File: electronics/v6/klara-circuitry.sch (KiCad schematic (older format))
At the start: 15 parts, among them J1 Pin header, U1 MCP1700-3302E, U3 ATtiny85

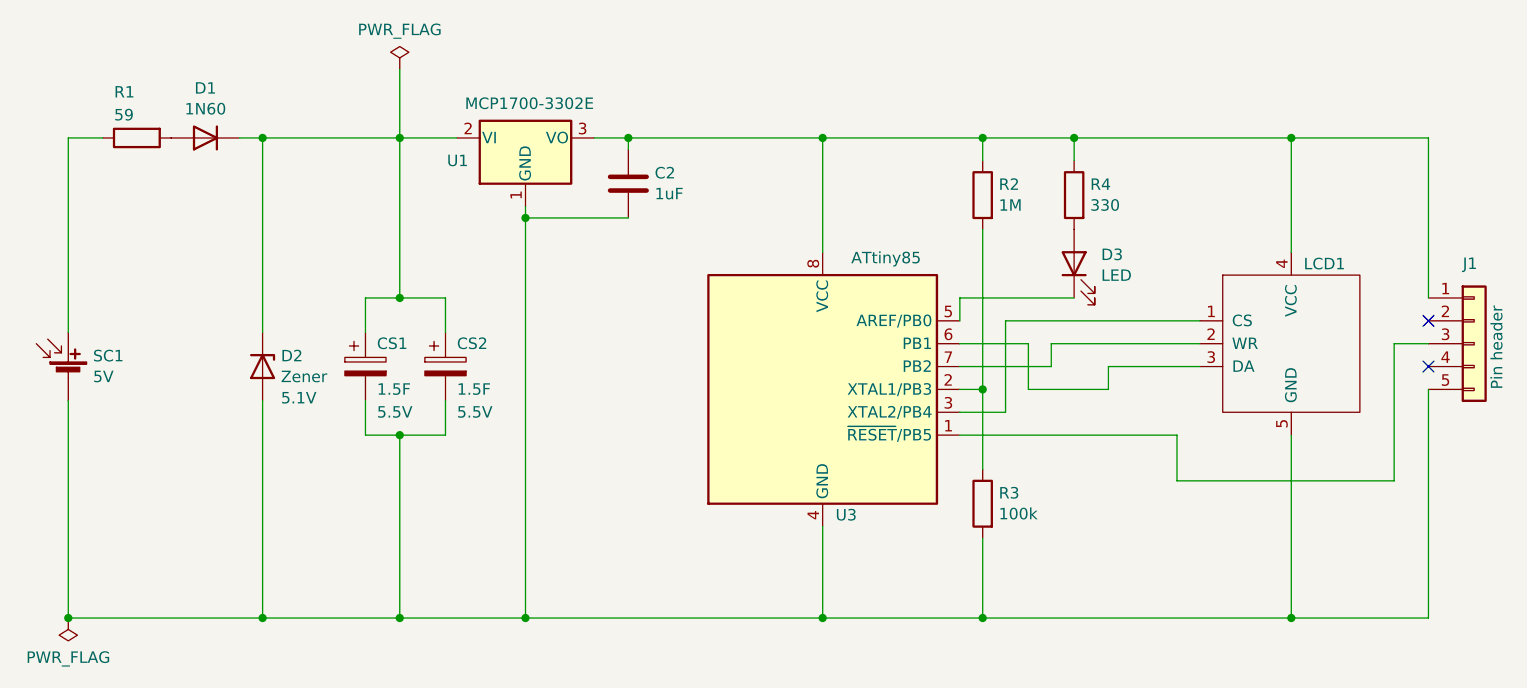
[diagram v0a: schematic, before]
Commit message: circuit d'oh: measure supercap voltage, not regulator output
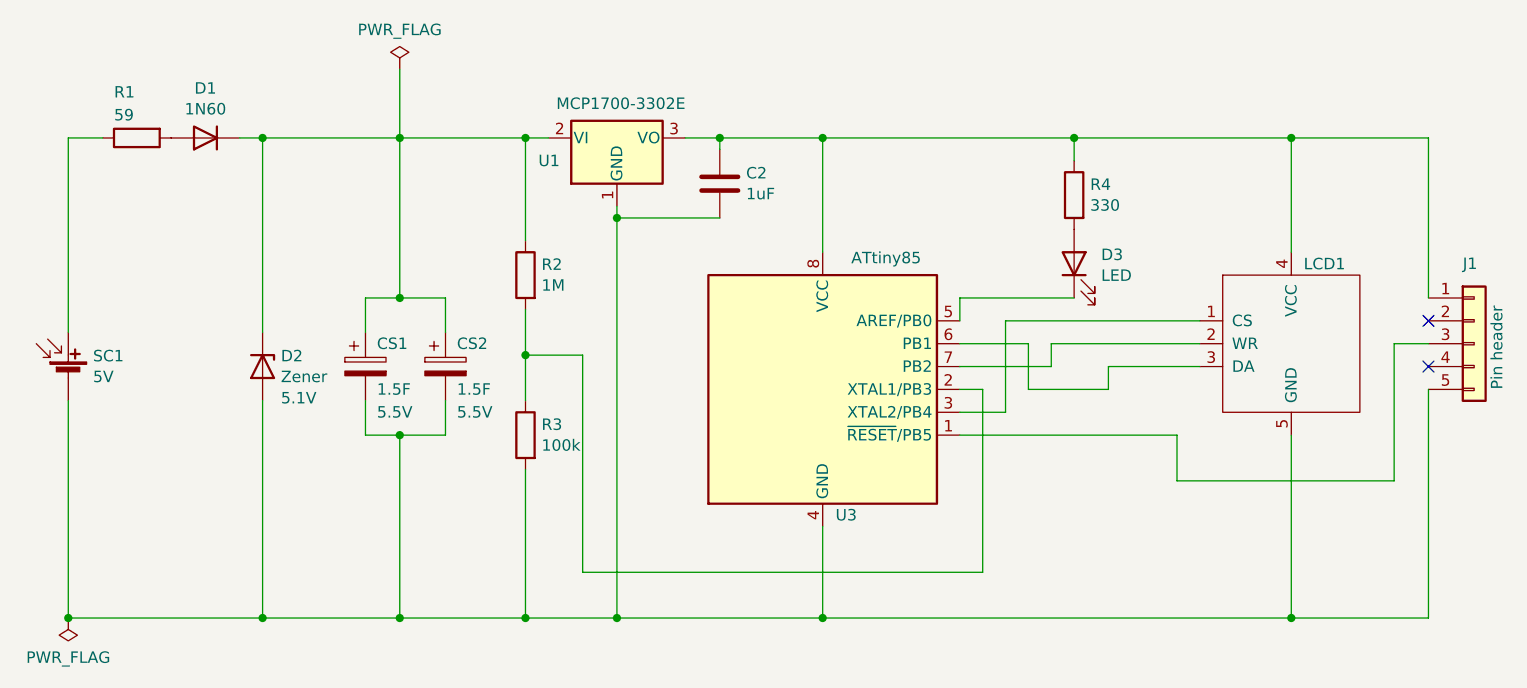
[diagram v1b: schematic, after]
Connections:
- net at C2.1, J1.1 (Pin_1), LCD1.4 (VCC)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: no longer R2.1
- net at CS1.1, CS2.1, D1.1 (K)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: now also R2.1
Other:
- moved on the sheet: C2, R2, R3, U1
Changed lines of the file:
@@
 L Regulator_Linear:MCP1700-3302E_TO92 U1
 U 1 1 62AF9A6C
-P 3500 1750
-F 0 "U1" H 3250 1850 50  0000 R CNN
-F 1 "MCP1700-3302E" H 3800 1600 50  0000 R CNN
-F 2 "Package_TO_SOT_THT:TO-92_Inline_Wide" H 3500 1550 50  0001 C CIN
-F 3 "http://ww1.microchip.com/downloads/en/DeviceDoc/20001826D.pdf" H 3500 1750 50  0001 C CNN
-	1    3500 1750
+P 3900 1750
+F 0 "U1" H 3650 1850 50  0000 R CNN
+F 1 "MCP1700-3302E" H 4200 1600 50  0000 R CNN
+F 2 "Package_TO_SOT_THT:TO-92_Inline_Wide" H 3900 1550 50  0001 C CIN
+F 3 "http://ww1.microchip.com/downloads/en/DeviceDoc/20001826D.pdf" H 3900 1750 50  0001 C CNN
+	1    3900 1750
 	1    0    0    1
 $EndComp
@@
 	5700 2850 5700 2650
 Wire Wire Line
-	3500 2050 3500 2100
+	3900 2050 3900 2100
 Wire Wire Line
 	5800 2650 5800 2750
@@
 $EndComp
 Wire Wire Line
-	4800 1750 5500 1750
-Wire Wire Line
-	3800 1750 3950 1750
+	4200 1750 4350 1750
 $Comp
 L Device:C C2
 U 1 1 62B08E4B
-P 3950 1950
-F 0 "C2" H 4065 1996 50  0000 L CNN
-F 1 "1uF" H 4065 1905 50  0000 L CNN
-F 2 "Capacitor_THT:C_Rect_L7.0mm_W2.0mm_P5.00mm" H 3988 1800 50  0001 C CNN
-F 3 "~" H 3950 1950 50  0001 C CNN
-	1    3950 1950
-	1    0    0    -1
-$EndComp
-Wire Wire Line
-	3950 1800 3950 1750
-Wire Wire Line
-	3950 2100 3500 2100
-Connection ~ 3500 2100
-Wire Wire Line
-	3500 2100 3500 3850
+P 4350 1950
+F 0 "C2" H 4465 1996 50  0000 L CNN
+F 1 "1uF" H 4465 1905 50  0000 L CNN
+F 2 "Capacitor_THT:C_Rect_L7.0mm_W2.0mm_P5.00mm" H 4388 1800 50  0001 C CNN
+F 3 "~" H 4350 1950 50  0001 C CNN
+	1    4350 1950
+	1    0    0    -1
+$EndComp
+Wire Wire Line
+	4350 1800 4350 1750
+Wire Wire Line
+	4350 2100 3900 2100
+Connection ~ 3900 2100
+Wire Wire Line
+	3900 2100 3900 3850
 $Comp
 L Device:R R2
 U 1 1 62B0AC42
-P 5500 2000
-F 0 "R2" H 5430 2046 50  0000 R CNN
-F 1 "1M" H 5430 1955 50  0000 R CNN
-F 2 "Resistor_THT:R_Axial_DIN0207_L6.3mm_D2.5mm_P10.16mm_Horizontal" V 5430 2000 50  0001 C CNN
-F 3 "~" H 5500 2000 50  0001 C CNN
-	1    5500 2000
+P 3500 2350
+F 0 "R2" H 3430 2396 50  0000 R CNN
+F 1 "1M" H 3430 2305 50  0000 R CNN
+F 2 "Resistor_THT:R_Axial_DIN0207_L6.3mm_D2.5mm_P10.16mm_Horizontal" V 3430 2350 50  0001 C CNN
+F 3 "~" H 3500 2350 50  0001 C CNN
+	1    3500 2350
 	-1   0    0    -1
 $EndComp
@@
 L Device:R R3
 U 1 1 62B0C047
-P 5500 3350
-F 0 "R3" H 5430 3396 50  0000 R CNN
-F 1 "100k" H 5430 3305 50  0000 R CNN
-F 2 "Resistor_THT:R_Axial_DIN0207_L6.3mm_D2.5mm_P10.16mm_Horizontal" V 5430 3350 50  0001 C CNN
-F 3 "~" H 5500 3350 50  0001 C CNN
-	1    5500 3350
+P 3500 3050
+F 0 "R3" H 3430 3096 50  0000 R CNN
+F 1 "100k" H 3430 3005 50  0000 R CNN
+F 2 "Resistor_THT:R_Axial_DIN0207_L6.3mm_D2.5mm_P10.16mm_Horizontal" V 3430 3050 50  0001 C CNN
+F 3 "~" H 3500 3050 50  0001 C CNN
+	1    3500 3050
 	-1   0    0    -1
 $EndComp
 Wire Wire Line
-	5500 1850 5500 1750
-Connection ~ 5500 1750
-Wire Wire Line
 	5400 2850 5500 2850
-Wire Wire Line
-	5500 2850 5500 2150
 Connection ~ 2350 3850
 Wire Wire Line
@@
 Connection ~ 2350 1750
 Wire Wire Line
-	5500 1750 5900 1750
-Wire Wire Line
 	5900 1850 5900 1750
 Wire Wire Line
@@
 Connection ~ 2950 3850
 Wire Wire Line
-	2950 3850 3500 3850
-Wire Wire Line
 	2950 2450 2950 1750
 Wire Wire Line
@@
 Connection ~ 2950 1750
 Wire Wire Line
-	2950 1750 3200 1750
-Wire Wire Line
 	6850 3850 7450 3850
 Connection ~ 6850 3850
@@
 	6850 1750 7450 1750
 Connection ~ 6850 1750
-Wire Wire Line
-	4800 3850 5500 3850
-Wire Wire Line
-	5500 2850 5500 3200
-Connection ~ 5500 2850
-Wire Wire Line
-	5500 3500 5500 3850
-Connection ~ 5500 3850
-Wire Wire Line
-	5500 3850 6850 3850
 $Comp
 L MCU_Microchip_ATtiny:ATtiny85-20PU U3
@@
 	5900 1750 6850 1750
 Wire Wire Line
-	3950 1750 4800 1750
-Connection ~ 3950 1750
+	4350 1750 4800 1750
+Connection ~ 4350 1750
 Connection ~ 4800 1750
-Wire Wire Line
-	3500 3850 4800 3850
-Connection ~ 3500 3850
 Connection ~ 4800 3850
 $Comp
@@
 NoConn ~ 7450 2550
 NoConn ~ 7450 2750
+Connection ~ 3900 3850
+Wire Wire Line
+	3900 3850 4800 3850
+Wire Wire Line
+	2950 3850 3500 3850
+Wire Wire Line
+	4800 1750 5900 1750
+Wire Wire Line
+	4800 3850 6850 3850
+Wire Wire Line
+	2950 1750 3500 1750
+Wire Wire Line
+	3500 2200 3500 1750
+Connection ~ 3500 1750
+Wire Wire Line
+	3500 1750 3600 1750
+Wire Wire Line
+	3500 2500 3500 2700
+Wire Wire Line
+	3500 3200 3500 3850
+Connection ~ 3500 3850
+Wire Wire Line
+	3500 3850 3900 3850
+Wire Wire Line
+	5500 3650 3750 3650
+Wire Wire Line
+	3750 3650 3750 2700
+Wire Wire Line
+	3750 2700 3500 2700
+Wire Wire Line
+	5500 2850 5500 3650
+Connection ~ 3500 2700
+Wire Wire Line
+	3500 2700 3500 2900
 $EndSCHEMATC
